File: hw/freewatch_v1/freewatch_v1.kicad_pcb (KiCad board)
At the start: 4 copper layers, 40 x 40 mm, 105 parts, among them P1 USB-MICRO-AB, P3 CONN_2, P6 CONN_2, P7 CONN_6, Q1 BSS138, Q2 BSS138, SW1 SW_PUSH, SW2 SW_PUSH, SW3 SW_PUSH, SW4 SW_PUSH, U1 PRTR5V0U2X, U10 MAX44009, U11 LSM303C, U12 MS5806-02BA, U13 ADP198, U14 LS013B7DH03, U15 EFM32GG330, U2 bq24072, U3 TPS780180300, U4 MAX17047, U5 TPS780180300, U6 M10478-A1, U7 MICRO_SDCARD_SPI, U8 ADP198, X1 CRYSTAL_SMD

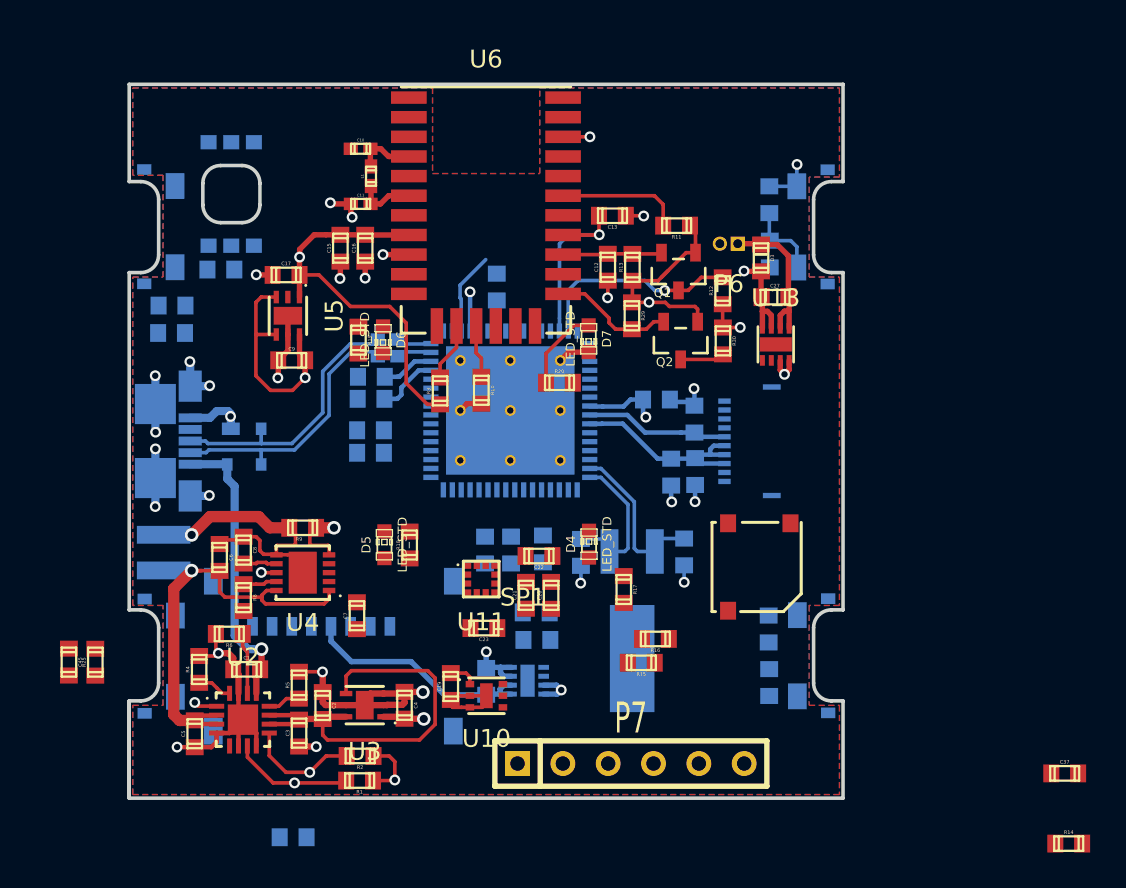
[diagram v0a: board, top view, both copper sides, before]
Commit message: hw: Add 48MHz crystal (required for USB) + footprint, continue routing.
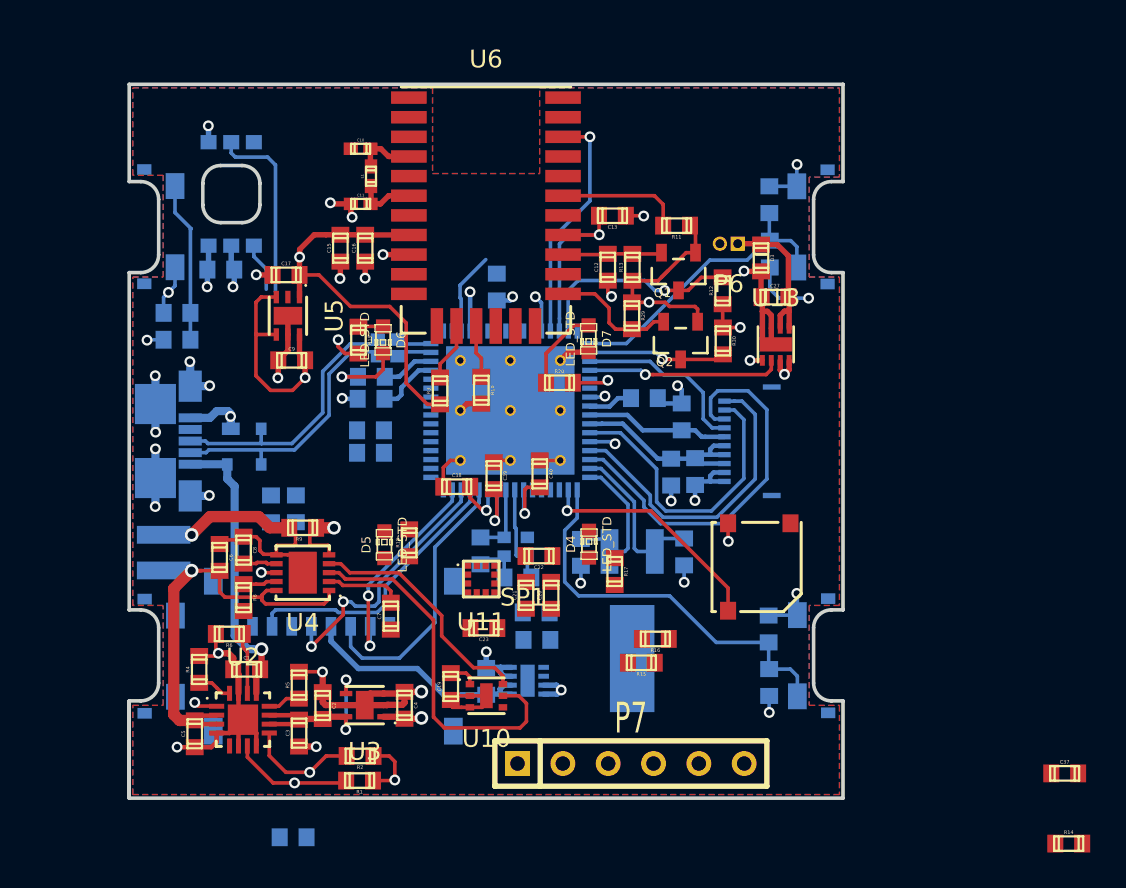
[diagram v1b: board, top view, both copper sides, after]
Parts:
- added C18: 10pF, Capacitors_SMD:c_0603, B.Cu at (108.1, 101.9)
- added C24: 10pF, Capacitors_SMD:c_0603, B.Cu at (106.0, 100.4)
- added X2: 48MHz, freewatch_footprints:ABM11_CRYSTAL, B.Cu at (108.0, 100.2)
- C38, C39, C40: moved to F.Cu
- C45, R25: moved to B.Cu
- X1: value CRYSTAL_SMD -> 32.768kHz
- moved C45 14.2 mm to (94.2, 98.1), turned to 90 degrees
- moved R25 14.1 mm to (95.6, 98.1), turned to 270 degrees
- moved C39 4.28 mm to (106.7, 96.2), turned to 270 degrees
- moved C40 4.21 mm to (109.3, 96.1), turned to 270 degrees
- moved C38 3.89 mm to (104.7, 96.8), turned to 0 degrees
- moved R23 1.94 mm to (89.0, 88.6)
- moved C7 1.90 mm to (101.0, 104.1)
- moved C43 1.17 mm to (89.0, 87.1)
- moved R17 1.13 mm to (113.5, 101.6)
- moved C30 0.73 mm to (117.3, 92.9)
- moved C41 0.68 mm to (115.2, 91.9)
- moved R18 0.12 mm to (102.0, 100.0)
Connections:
- U15 pad 12: Net-(U15-Pad12) -> SD_EN
- U15 pad 24: LS_INT_N -> Net-(C18-Pad1)
- U15 pad 25: SD_EN -> Net-(C24-Pad1)
- U15 pad 7: Net-(U15-Pad7) -> LS_INT_N
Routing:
- net SCL: track 0.00 -> 31.0 mm
- net GND: track 82.8 -> 110.3 mm, vias 31 -> 38
- net /MCU_DISPLAY/LCD_BKL1: track 0.00 -> 24.2 mm, vias 0 -> 3
- net /MCU_DISPLAY/SW_BR: track 0.00 -> 22.7 mm
- net /MCU_DISPLAY/LCD_CS: track 0.00 -> 22.1 mm
- net VCC: track 30.4 -> 50.0 mm, vias 7 -> 15
- net /MCU_DISPLAY/LCD_CLK: track 0.00 -> 17.7 mm
- net /MCU_DISPLAY/LCD_DI: track 0.00 -> 16.9 mm
- net SDA: track 0.00 -> 16.2 mm
- net SD_MISO: track 0.00 -> 15.8 mm
- net SD_MOSI: track 0.00 -> 15.4 mm
- net SD_CLK: track 0.00 -> 14.8 mm, vias 0 -> 2
- net /MCU_DISPLAY/BUZ: track 0.00 -> 13.3 mm, vias 0 -> 1
- net /MCU_DISPLAY/SW_TR: track 4.37 -> 17.2 mm
- net Net-(C2-Pad1): track 22.9 -> 10.7 mm, vias 0 -> 2
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
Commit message: hw: routing...
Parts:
- C33, C35: moved to F.Cu
- moved R7 14.8 mm to (95.9, 101.7)
- moved C33 4.40 mm to (104.2, 93.7), turned to 180 degrees
- moved R18 2.84 mm to (99.4, 98.9)
- moved C35 1.30 mm to (99.5, 90.7)
- moved C34 1.02 mm to (98.9, 94.5)
- moved C23 0.58 mm to (106.2, 104.2)
- moved R28 0.54 mm to (108.6, 103.8)
- moved C42 0.46 mm to (107.4, 85.7)
- moved R27 0.46 mm to (108.7, 105.4)
- moved C36 0.41 mm to (99.5, 90.7)
- moved D4 0.06 mm to (112.1, 100.0), turned to 270 degrees
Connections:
- U15 pad 19: AC_INT_XL -> AC_INT_MAG
- U15 pad 33: AC_INT_MAG -> AC_INT_XL
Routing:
- net SDA: track 16.2 -> 44.2 mm, vias 0 -> 1
- net USB_ID: track 0.00 -> 25.4 mm, vias 0 -> 2
- net SCL: track 31.0 -> 55.5 mm, vias 0 -> 3
- net /MCU_DISPLAY/SW_BL: track 0.00 -> 21.2 mm
- net /MCU_DISPLAY/MCU_RST_N: track 0.00 -> 20.9 mm, vias 0 -> 1
- net AC_SDIO: track 0.00 -> 20.2 mm, vias 0 -> 1
- net AC_CS_MAG: track 0.00 -> 18.1 mm, vias 0 -> 1
- net AC_CS_XL: track 0.00 -> 16.0 mm, vias 0 -> 1
- net AC_CLK: track 0.00 -> 14.7 mm, vias 0 -> 1
- net AC_INT_MAG: track 0.00 -> 12.6 mm, vias 0 -> 1
- net GND: track 110.3 -> 120.4 mm, vias 38 -> 43
- net AC_INT_XL: track 0.00 -> 7.90 mm, vias 0 -> 1
- net GPS_RST: track 0.00 -> 7.38 mm, vias 0 -> 1
- net /MCU_DISPLAY/SW_TL: track 9.00 -> 16.1 mm
- net FG_ALRT_N: track 0.86 -> 7.00 mm
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
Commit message: hw: still routing.
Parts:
- moved R14 62.2 mm to (83.5, 88.6)
- moved C37 36.0 mm to (103.0, 116.8)
- moved R16 4.84 mm to (112.3, 108.7), turned to 0 degrees
- moved R10 3.07 mm to (103.0, 91.2), turned to 180 degrees
- moved R15 2.41 mm to (112.7, 105.9), turned to 0 degrees
- moved R3 1.89 mm to (102.7, 89.9), turned to 0 degrees
- moved R19 1.73 mm to (98.5, 87.0), turned to 180 degrees
- moved P7 0.27 mm to (114.7, 112.3), turned to 180 degrees
- moved C19 0.15 mm to (104.2, 108.2)
- moved C42 0.12 mm to (107.2, 85.7)
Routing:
- net /MCU_DISPLAY/SWCLK: track 2.18 -> 49.9 mm, vias 1 -> 2
- net /MCU_DISPLAY/SWDO: track 2.39 -> 47.1 mm, vias 1 -> 2
- net /MCU_DISPLAY/SWDIO: track 2.15 -> 46.7 mm, vias 1 -> 2
- net SD_EN: track 1.47 -> 34.4 mm, vias 1 -> 2
- net LS_INT_N: track 0.88 -> 33.8 mm, vias 1 -> 3
- net /MCU_DISPLAY/LCD_BKL2: track 2.57 -> 27.6 mm, vias 1 -> 2
- net +5V: track 23.1 -> 45.8 mm
- net /MCU_DISPLAY/SW_TL: track 16.1 -> 29.6 mm, vias 0 -> 2
- net VCC: track 56.0 -> 66.9 mm, vias 17 -> 22
- net SCL: track 55.5 -> 65.0 mm, vias 3 -> 4
- net SDA: track 44.2 -> 51.7 mm, vias 1 -> 2
- net GND: track 120.4 -> 127.9 mm, vias 43 -> 44
- net /MCU_DISPLAY/LCD_BKL1: track 25.0 -> 29.3 mm, vias 3 -> 6
- net /MCU_DISPLAY/MCU_RST_N: track 20.9 -> 17.4 mm, vias 1 -> 0
- net +1.8V: track 55.5 -> 52.1 mm
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
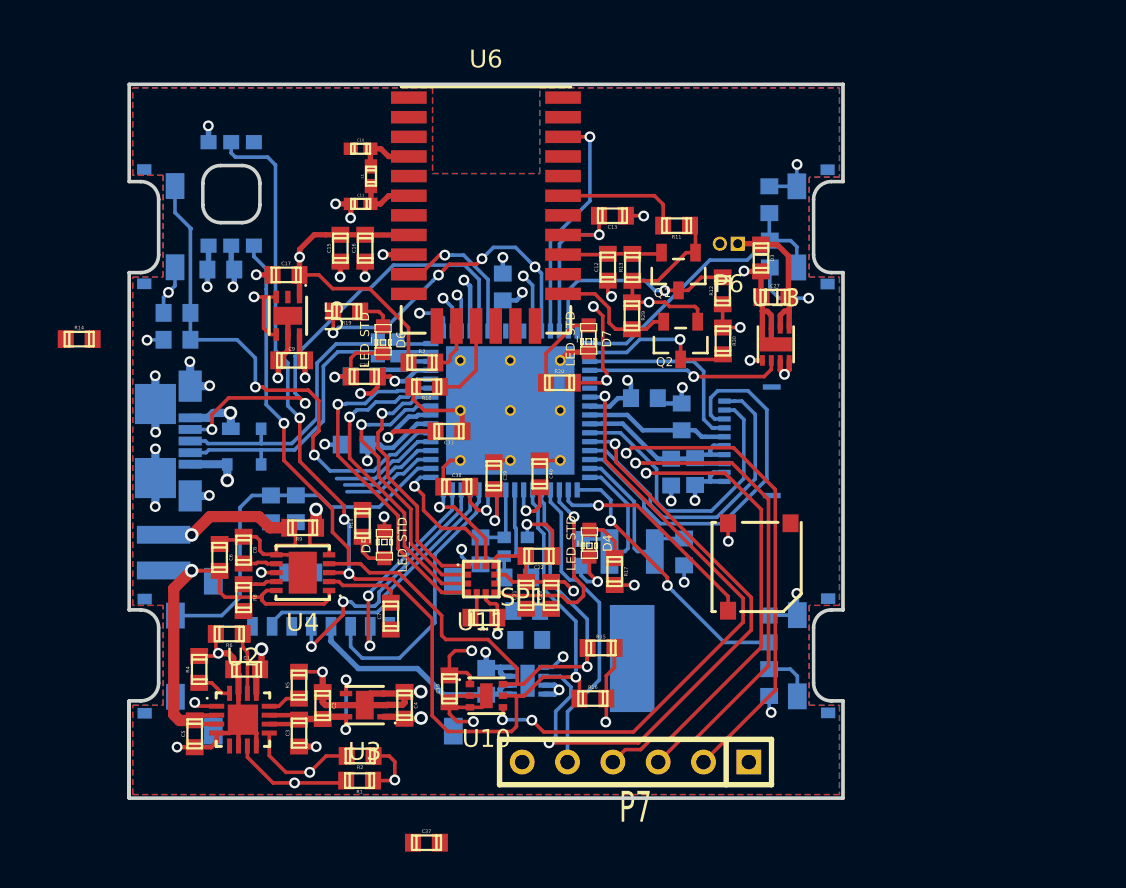
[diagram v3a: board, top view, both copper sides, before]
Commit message: hw: Cleanup schematics, routing almost finished.
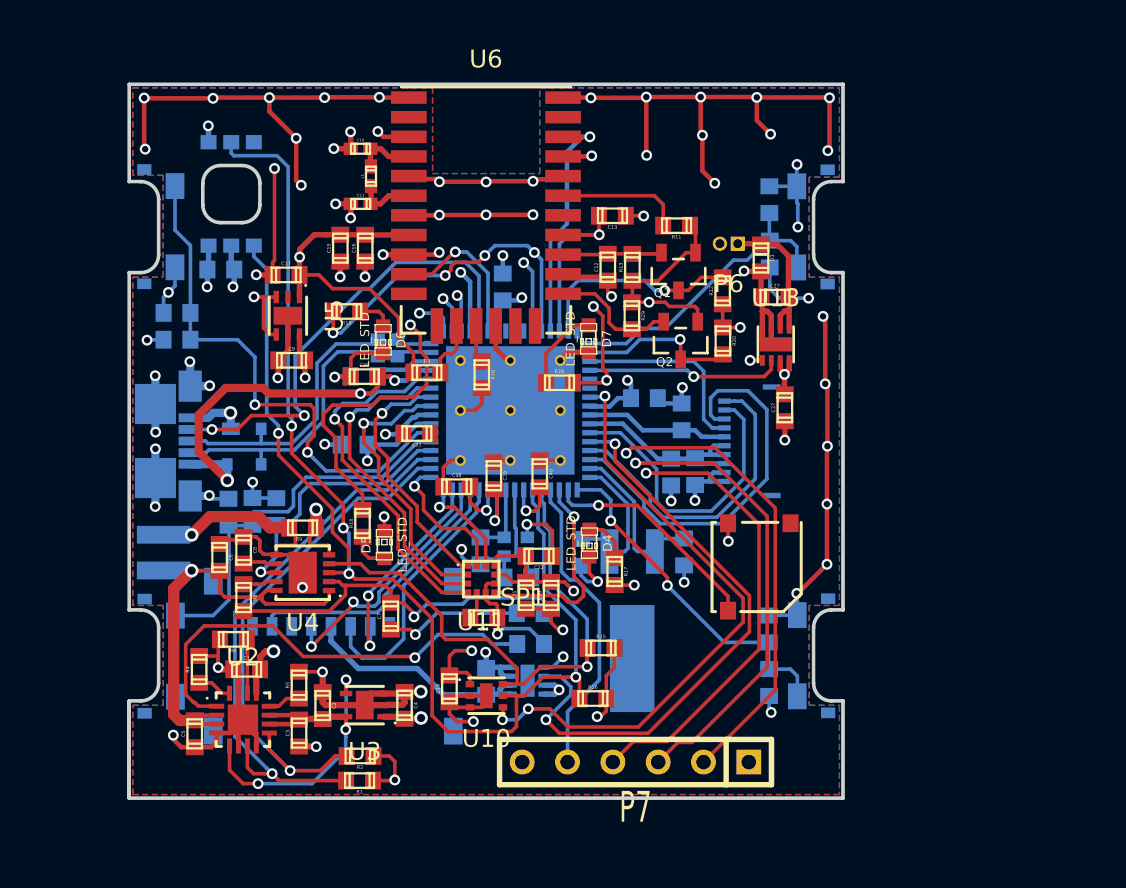
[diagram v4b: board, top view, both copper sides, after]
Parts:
- removed R14: 4k7, freewatch_footprints:r_0603
- moved C37 31.6 mm to (123.0, 92.4), turned to 90 degrees
- moved R7 3.68 mm to (94.5, 98.2), turned to 270 degrees
- moved R10 3.16 mm to (106.1, 90.6), turned to 270 degrees
- moved R25 2.43 mm to (93.2, 98.2), turned to 90 degrees
- moved C45 2.39 mm to (91.9, 98.3), turned to 270 degrees
- moved C33 1.81 mm to (102.4, 93.9)
- moved R3 0.62 mm to (103.0, 90.4)
- moved R6 0.38 mm to (92.1, 105.4)
- moved R27 0.25 mm to (108.8, 105.7)
- moved R28 0.23 mm to (108.8, 103.9), turned to 180 degrees
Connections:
- U15 pad 34: /MCU_DISPLAY/SW_BL -> BC_CHG_N
- U15 pad 36: BC_CHG_N -> FG_ALRT_N
- U15 pad 37: FG_ALRT_N -> /MCU_DISPLAY/SW_BL
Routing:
- net GND: track 127.9 -> 240.6 mm, vias 44 -> 82
- net /MCU_DISPLAY/LCD_BKL2: track 27.6 -> 54.3 mm, vias 2 -> 3
- net Net-(R27-Pad2): track 1.31 -> 25.3 mm
- net BC_PGOOD_N: track 12.3 -> 31.5 mm
- net BC_CHG_N: track 12.0 -> 29.9 mm
- net Net-(C7-Pad1): track 4.33 -> 21.2 mm, vias 0 -> 1
- net Net-(C6-Pad2): track 16.6 -> 32.6 mm, vias 1 -> 3
- net Net-(C2-Pad1): track 10.7 -> 20.8 mm, vias 2 -> 3
- net FG_ALRT_N: track 7.00 -> 14.9 mm
- net +5V: track 45.8 -> 50.5 mm
- net VCC: track 66.9 -> 69.9 mm, vias 22 -> 23
- net Net-(R10-Pad2): track 4.88 -> 2.11 mm
- net Net-(C33-Pad1): track 5.74 -> 3.00 mm
- net /MCU_DISPLAY/LCD_BKL1: track 29.3 -> 31.0 mm
- net SD_EN: track 34.4 -> 33.4 mm
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- added copper zone on B.Cu, net GND
- removed copper zone on B.Cu, net VCC

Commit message: hw: Add mounting holes. Check with Eurocircuits PCB analyzer.
-> problem with vias OAR and IAR, to be investigated.
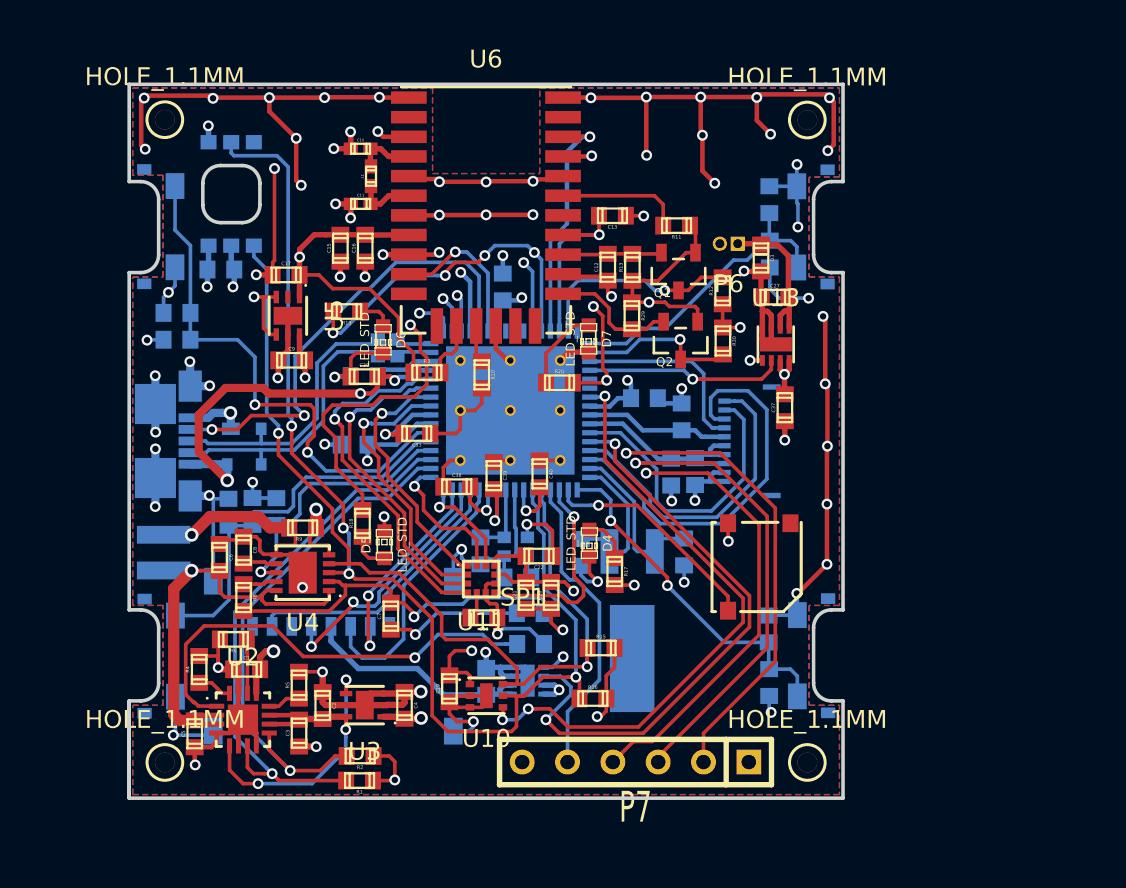
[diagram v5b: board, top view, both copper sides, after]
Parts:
- added HOLE_1.1MM: VAL**, freewatch_footprints:HOLE_1.1MM, F.Cu at (88.3, 112.3)
- added HOLE_1.1MM: VAL**, freewatch_footprints:HOLE_1.1MM, F.Cu at (124.3, 112.3)
- added HOLE_1.1MM: VAL**, freewatch_footprints:HOLE_1.1MM, F.Cu at (124.3, 76.3)
- added HOLE_1.1MM: VAL**, freewatch_footprints:HOLE_1.1MM, F.Cu at (88.3, 76.3)
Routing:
- net GND: track 240.6 -> 258.9 mm, vias 82 -> 83
- net Net-(C33-Pad1): track 3.00 -> 4.02 mm

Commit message: hw: Change via sizes to millimeters (in design rules).
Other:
- net class Default: via_dia 0.889 -> 1; via_drill 0.635 -> 0.6
- net class class3: via_dia 1.0668 -> 1; via_drill 0.6604 -> 0.6
- net class class4: via_dia 0.762 -> 0.75; via_drill 0.4572 -> 0.45
- net class class5: via_dia 0.762 -> 0.75; via_drill 0.4572 -> 0.45
- net class class6: via_dia 0.6096 -> 0.6; via_drill 0.3556 -> 0.35
- rule via_min_drill: 0.3556 -> 0.35
- rule via_min_size: 0.6096 -> 0.6

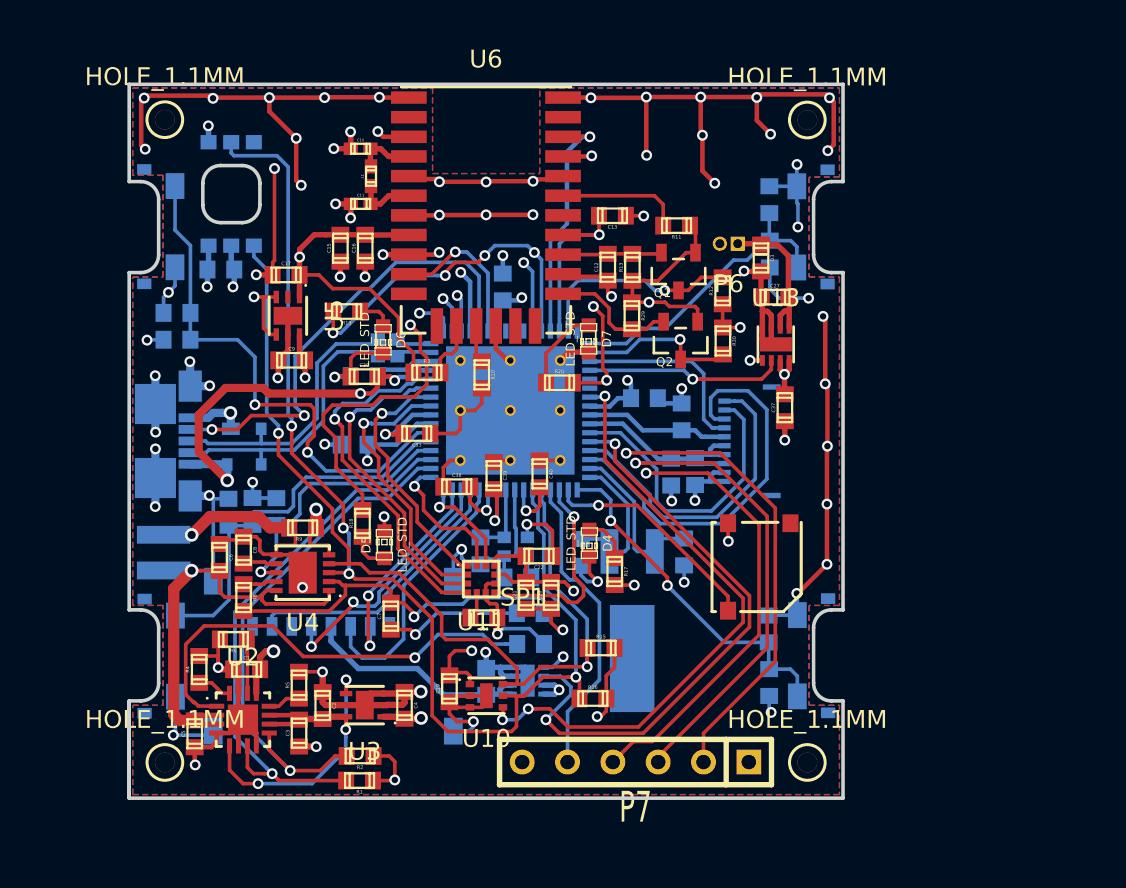
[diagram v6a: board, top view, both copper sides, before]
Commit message: hw: change vias hole sizes to finished diameter (to pass Eurocircuits DRC).
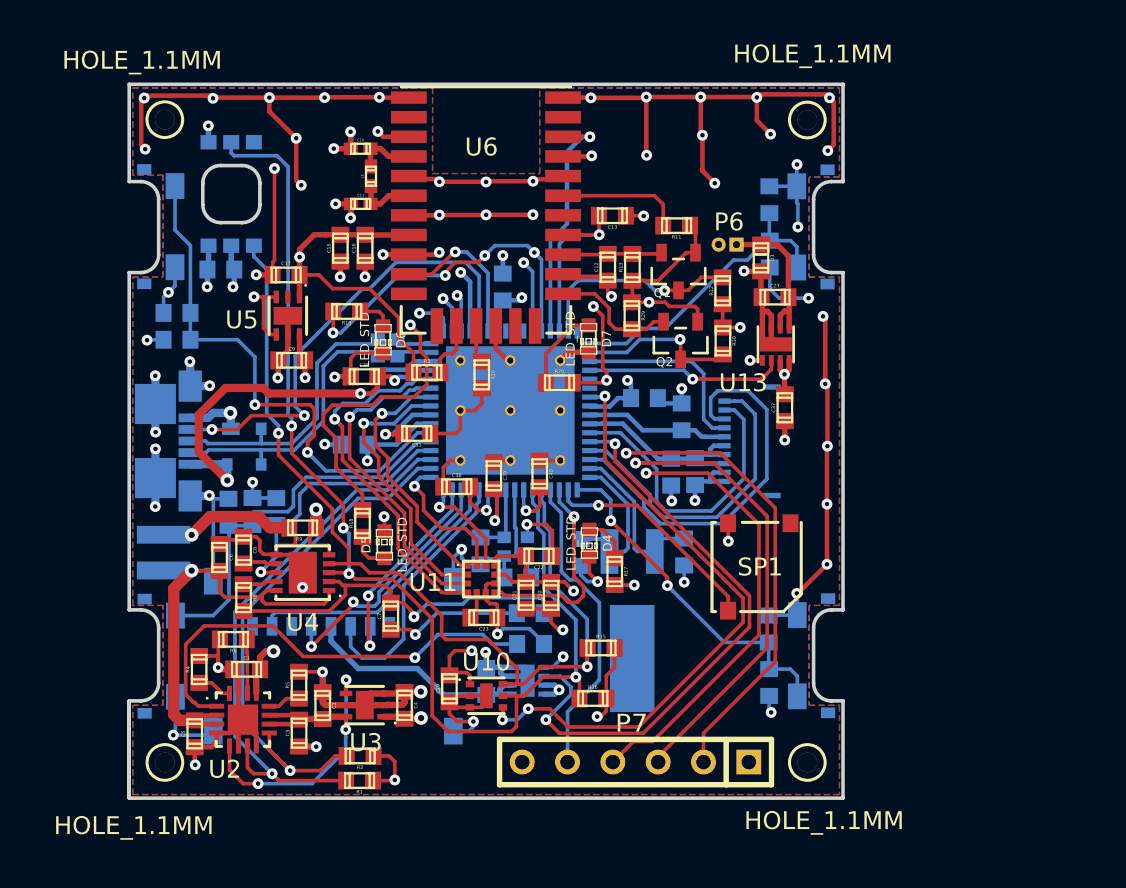
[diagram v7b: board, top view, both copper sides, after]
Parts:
- moved P6 0.09 mm to (119.8, 83.3)
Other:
- net class Default: via_drill 0.6 -> 0.5
- net class class3: via_drill 0.6 -> 0.5
- net class class4: via_drill 0.45 -> 0.35
- net class class5: via_drill 0.45 -> 0.35
- net class class6: via_drill 0.35 -> 0.25
- rule via_min_drill: 0.35 -> 0.25
